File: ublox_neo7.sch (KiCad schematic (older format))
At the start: 1 part, among them U4 ublox_neo7

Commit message: added lots of stuff
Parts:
- added C30: CP, alis_parts:DSK-3R3H204T614-H2L, symbol CP
- added D10: D_Schottky, Diodes_SMD:SOD-323, symbol D_Schottky
- added R7: 100R, Resistors_SMD:R_0402, symbol R
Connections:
- net GND: now also C30.2
- net VCC: now also D10.2 (A)
- net V_BCKP: now also C30.1, R7.1
- new net: D10.1 (K), R7.2
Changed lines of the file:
@@
 EESchema Schematic File Version 2
+LIBS:stm32f4_lqfp64_mpu6050-rescue
 LIBS:power
 LIBS:device
@@
 LIBS:minimal
 LIBS:alis_parts
+LIBS:sensors
+LIBS:stm32
 LIBS:stm32f4_lqfp64_mpu6050-cache
 EELAYER 25 0
@@
 $Descr A4 11693 8268
 encoding utf-8
-Sheet 7 7
+Sheet 7 10
 Title ""
 Date ""
@@
 Comment4 ""
 $EndDescr
-Text GLabel 4700 4250 0    60   Input ~ 0
+Text GLabel 3900 4250 0    60   Input ~ 0
 V_BCKP
 Wire Wire Line
@@
 	4600 2250 4600 4750
 Wire Wire Line
-	4700 4650 4600 4650
+	4050 4650 4700 4650
 Connection ~ 6500 2650
 Wire Wire Line
@@
 	6400 3450 6500 3450
 $Comp
-L GND #PWR24
+L GND #PWR23
 U 1 1 569BAFB4
 P 6500 3550
-F 0 "#PWR24" H 6500 3300 50  0001 C CNN
+F 0 "#PWR23" H 6500 3300 50  0001 C CNN
 F 1 "GND" H 6508 3376 50  0000 C CNN
 F 2 "" H 6500 3550 50  0000 C CNN
@@
 $EndComp
 $Comp
-L GND #PWR25
+L GND #PWR32
 U 1 1 569BAFBA
 P 4600 4750
-F 0 "#PWR25" H 4600 4500 50  0001 C CNN
+F 0 "#PWR32" H 4600 4500 50  0001 C CNN
 F 1 "GND" H 4608 4576 50  0000 C CNN
 F 2 "" H 4600 4750 50  0000 C CNN
@@
 	1    0    0    -1
 $EndComp
+$Comp
+L CP C30
+U 1 1 569C06BB
+P 4050 4400
+F 0 "C30" H 4168 4446 50  0000 L CNN
+F 1 "CP" H 4168 4354 50  0000 L CNN
+F 2 "alis_parts:DSK-3R3H204T614-H2L" H 4088 4250 50  0001 C CNN
+F 3 "" H 4050 4400 50  0000 C CNN
+	1    4050 4400
+	1    0    0    -1
+$EndComp
+Wire Wire Line
+	3900 4250 4700 4250
+Connection ~ 4050 4250
+Wire Wire Line
+	4050 4550 4050 4650
+$Comp
+L D_Schottky D10
+U 1 1 569C080A
+P 3600 3950
+F 0 "D10" H 3600 3733 50  0000 C CNN
+F 1 "D_Schottky" H 3600 3825 50  0000 C CNN
+F 2 "Diodes_SMD:SOD-323" H 3600 3950 50  0001 C CNN
+F 3 "" H 3600 3950 50  0000 C CNN
+	1    3600 3950
+	-1   0    0    1
+$EndComp
+Wire Wire Line
+	4050 3950 4050 4250
+Text GLabel 3450 3950 0    60   Input ~ 0
+VCC
+$Comp
+L R R7
+U 1 1 569D5B11
+P 3900 3950
+F 0 "R7" V 3692 3950 50  0000 C CNN
+F 1 "100R" V 3784 3950 50  0000 C CNN
+F 2 "Resistors_SMD:R_0402" V 3830 3950 50  0001 C CNN
+F 3 "" H 3900 3950 50  0000 C CNN
+	1    3900 3950
+	0    1    1    0
+$EndComp
 $EndSCHEMATC

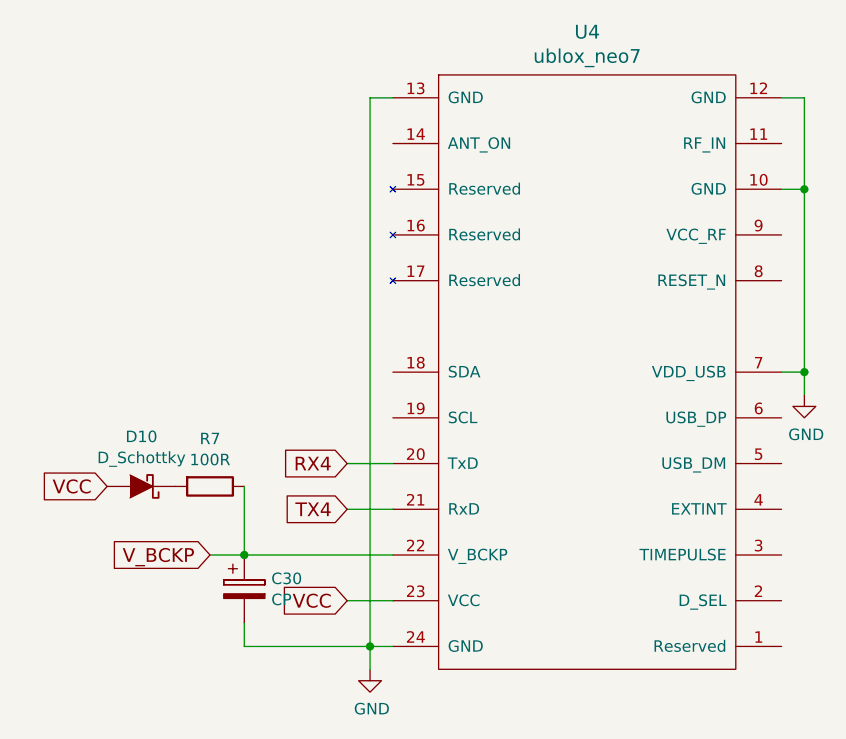
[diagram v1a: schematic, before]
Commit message: changed some netnames
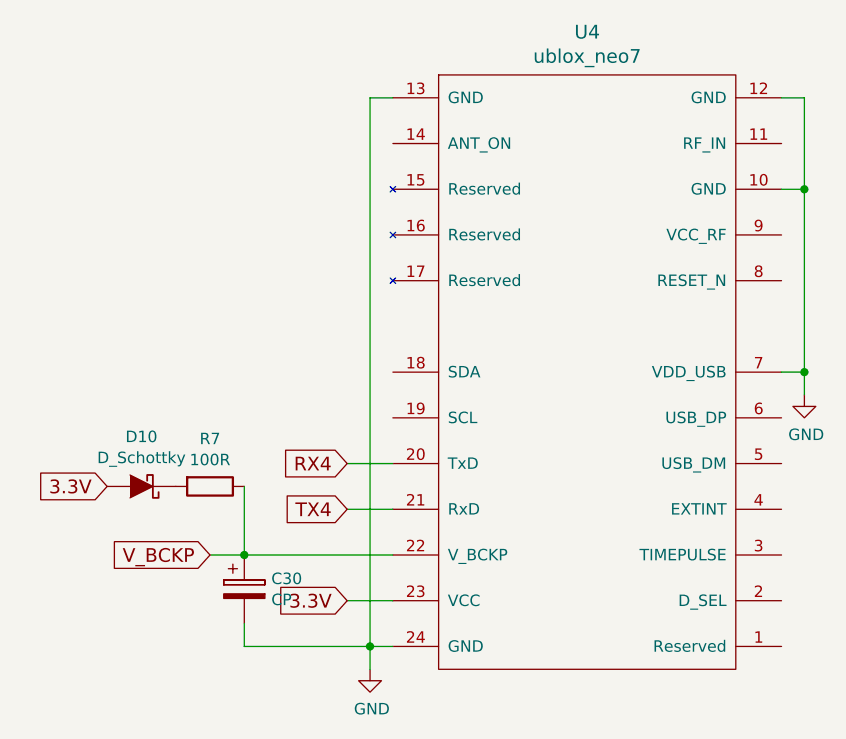
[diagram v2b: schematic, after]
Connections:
- net VCC renamed 3.3V
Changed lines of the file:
@@
 	4500 4450 4700 4450
 Text GLabel 4500 4450 0    60   Input ~ 0
-VCC
+3.3V
 Connection ~ 4600 4650
 Wire Wire Line
@@
 	4050 3950 4050 4250
 Text GLabel 3450 3950 0    60   Input ~ 0
-VCC
+3.3V
 $Comp
 L R R7
